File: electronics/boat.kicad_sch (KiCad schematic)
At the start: 22 parts, among them J2 UART1, M5 SG90 9g Micro Servo, M9 WaterPump_DC_DelavanAgPumpsDi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, SW1 Reset, U11 TLE5206-2S, U2 PIC32MX170F256B

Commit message: gate and water pump schematic updated according to wiring
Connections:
- net ConnectionIndicatorPWM4: now also U2.6 (RB2); no longer U2.9 (RA2)
- net GatePWM3: no longer U2.10 (RA3)
- new net GatePWM5: U2.9 (RA2)
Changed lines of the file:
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@@
+	)
+	(no_connect
+		(at 50.8 73.66)
 	)
 	(no_connect
@@
 	)
 	(no_connect
-		(at 90.17 62.23)
-	)
-	(no_connect
 		(at 198.12 90.17)
 	)
@@
 	(wire
 		(pts
+			(xy 114.046 69.85) (xy 118.11 69.85)
+		)
+		(stroke
+			(width 0)
+			(type default)
+		)
+	)
+	(wire
+		(pts
+			(xy 127 45.72) (xy 127 52.07)
+		)
+		(stroke
+			(width 0)
+			(type default)
+		)
+	)
+	(wire
+		(pts
+			(xy 48.26 68.58) (xy 50.8 68.58)
+		)
+		(stroke
+			(width 0)
+			(type default)
+		)
+	)
+	(wire
+		(pts
+			(xy 118.11 69.85) (xy 118.11 70.104)
+		)
+		(stroke
+			(width 0)
+			(type default)
+		)
+	)
+	(wire
+		(pts
+			(xy 130.81 25.146) (xy 130.81 49.53)
+		)
+		(stroke
+			(width 0)
+			(type default)
+		)
+	)
+	(wire
+		(pts
+			(xy 231.14 95.25) (xy 231.14 96.52)
+		)
+		(stroke
+			(width 0)
+			(type default)
+		)
+	)
+	(wire
+		(pts
+			(xy 226.06 38.1) (xy 226.06 41.91)
+		)
+		(stroke
+			(width 0)
+			(type default)
+		)
+	)
+	(wire
+		(pts
+			(xy 201.676 138.43) (xy 204.978 138.43)
+		)
+		(stroke
+			(width 0)
+			(type default)
+		)
+	)
+	(wire
+		(pts
+			(xy 50.8 135.89) (xy 50.8 138.43)
+		)
+		(stroke
+			(width 0)
+			(type default)
+		)
+	)
+	(wire
+		(pts
+			(xy 90.17 25.146) (xy 90.17 40.894)
+		)
+		(stroke
+			(width 0)
+			(type default)
+		)
+	)
+	(wire
+		(pts
+			(xy 204.978 143.51) (xy 209.042 143.51)
+		)
+		(stroke
+			(width 0)
+			(type default)
+		)
+	)
+	(wire
+		(pts
+			(xy 228.6 95.25) (xy 228.6 96.52)
+		)
+		(stroke
+			(width 0)
+			(type default)
+		)
+	)
+	(wire
+		(pts
+			(xy 168.91 138.43) (xy 168.91 141.224)
+		)
+		(stroke
+			(width 0)
+			(type default)
+		)
+	)
+	(wire
+		(pts
+			(xy 104.14 156.21) (xy 74.93 156.21)
+		)
+		(stroke
+			(width 0)
+			(type default)
+		)
+	)
+	(wire
+		(pts
 			(xy 48.26 71.12) (xy 50.8 71.12)
 		)
@@
 	(wire
 		(pts
-			(xy 114.046 69.85) (xy 118.11 69.85)
-		)
-		(stroke
-			(width 0)
-			(type default)
-		)
-	)
-	(wire
-		(pts
-			(xy 127 45.72) (xy 127 52.07)
-		)
-		(stroke
-			(width 0)
-			(type default)
-		)
-	)
-	(wire
-		(pts
-			(xy 48.26 68.58) (xy 50.8 68.58)
-		)
-		(stroke
-			(width 0)
-			(type default)
-		)
-	)
-	(wire
-		(pts
-			(xy 118.11 69.85) (xy 118.11 70.104)
-		)
-		(stroke
-			(width 0)
-			(type default)
-		)
-	)
-	(wire
-		(pts
-			(xy 130.81 25.146) (xy 130.81 49.53)
-		)
-		(stroke
-			(width 0)
-			(type default)
-		)
-	)
-	(wire
-		(pts
-			(xy 231.14 95.25) (xy 231.14 96.52)
-		)
-		(stroke
-			(width 0)
-			(type default)
-		)
-	)
-	(wire
-		(pts
-			(xy 226.06 38.1) (xy 226.06 41.91)
-		)
-		(stroke
-			(width 0)
-			(type default)
-		)
-	)
-	(wire
-		(pts
-			(xy 201.676 138.43) (xy 204.978 138.43)
-		)
-		(stroke
-			(width 0)
-			(type default)
-		)
-	)
-	(wire
-		(pts
-			(xy 50.8 135.89) (xy 50.8 138.43)
-		)
-		(stroke
-			(width 0)
-			(type default)
-		)
-	)
-	(wire
-		(pts
-			(xy 90.17 25.146) (xy 90.17 40.894)
-		)
-		(stroke
-			(width 0)
-			(type default)
-		)
-	)
-	(wire
-		(pts
-			(xy 204.978 143.51) (xy 209.042 143.51)
-		)
-		(stroke
-			(width 0)
-			(type default)
-		)
-	)
-	(wire
-		(pts
-			(xy 228.6 95.25) (xy 228.6 96.52)
-		)
-		(stroke
-			(width 0)
-			(type default)
-		)
-	)
-	(wire
-		(pts
-			(xy 168.91 138.43) (xy 168.91 141.224)
-		)
-		(stroke
-			(width 0)
-			(type default)
-		)
-	)
-	(wire
-		(pts
-			(xy 104.14 156.21) (xy 74.93 156.21)
-		)
-		(stroke
-			(width 0)
-			(type default)
-		)
-	)
-	(wire
-		(pts
 			(xy 48.26 156.21) (xy 50.8 156.21)
 		)
@@
 	(wire
 		(pts
-			(xy 48.26 73.66) (xy 50.8 73.66)
-		)
-		(stroke
-			(width 0)
-			(type default)
-		)
-	)
-	(wire
-		(pts
 			(xy 202.946 116.078) (xy 202.946 125.984)
 		)
@@
 		(pts
 			(xy 48.26 133.35) (xy 50.8 133.35)
+		)
+		(stroke
+			(width 0)
+			(type default)
+		)
+	)
+	(wire
+		(pts
+			(xy 90.17 62.23) (xy 92.71 62.23)
 		)
 		(stroke
@@
 		)
 	)
+	(global_label "ConnectionIndicatorPWM4"
+		(shape input)
+		(at 92.71 62.23 0)
+		(fields_autoplaced yes)
+		(effects
+			(font
+				(size 1.27 1.27)
+			)
+			(justify left)
+		)
+		(property "Intersheetrefs" "${INTERSHEET_REFS}"
+			(at 120.0063 62.23 0)
+			(effects
+				(font
+					(size 1.27 1.27)
+				)
+				(justify left)
+				(hide yes)
+			)
+		)
+	)
 	(global_label "RX"
 		(shape output)
@@
 		)
 	)
-	(global_label "ConnectionIndicatorPWM4"
-		(shape input)
-		(at 48.26 71.12 180)
-		(fields_autoplaced yes)
-		(effects
-			(font
-				(size 1.27 1.27)
-			)
-			(justify right)
-		)
-		(property "Intersheetrefs" "${INTERSHEET_REFS}"
-			(at 20.9637 71.12 0)
-			(effects
-				(font
-					(size 1.27 1.27)
-				)
-				(justify right)
-				(hide yes)
-			)
-		)
-	)
 	(global_label "UART2RX"
 		(shape output)
@@
 		)
 	)
+	(global_label "GatePWM5"
+		(shape input)
+		(at 48.26 71.12 180)
+		(fields_autoplaced yes)
+		(effects
+			(font
+				(size 1.27 1.27)
+			)
+			(justify right)
+		)
+		(property "Intersheetrefs" "${INTERSHEET_REFS}"
+			(at 35.6592 71.12 0)
+			(effects
+				(font
+					(size 1.27 1.27)
+				)
+				(justify right)
+				(hide yes)
+			)
+		)
+	)
 	(global_label "ConnectionIndicatorPWM4"
 		(shape output)
@@
 			(effects
 				(font
-					(size 1.27 1.27)
-				)
-				(justify right)
-				(hide yes)
-			)
-		)
-	)
-	(global_label "GatePWM3"
-		(shape input)
-		(at 48.26 73.66 180)
-		(fields_autoplaced yes)
-		(effects
-			(font
-				(size 1.27 1.27)
-			)
-			(justify right)
-		)
-		(property "Intersheetrefs" "${INTERSHEET_REFS}"
-			(at 35.6592 73.66 0)
-			(effects
-				(font

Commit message: water pump schematic updated to be driven by IRLZ34N N-channel MOSFET
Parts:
- removed C24: 470uF, symbol ME218_BaseLib:Cap
- removed C25: 0.1uF, symbol ME218_BaseLib:Cap
- removed U11: TLE5206-2S, TLE5206-2S:TO127P1000X440X1730-7, symbol TLE5206-2S:TLE5206-2S
- added Q1: IRLZ34N, Package_TO_SOT_THT:TO-220-3_Vertical, symbol Transistor_FET:IRLZ34N
- gave numbers to parts that had none: 5
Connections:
- net +14V: now also M9.1 (+)
- net GND: now also Q1.3 (S)
- net WaterPump: now also Q1.1 (G)
- net at M9.2 (-): now also Q1.2 (D)
- no-connect marks 30 -> 29
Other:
- moved on the sheet: M9

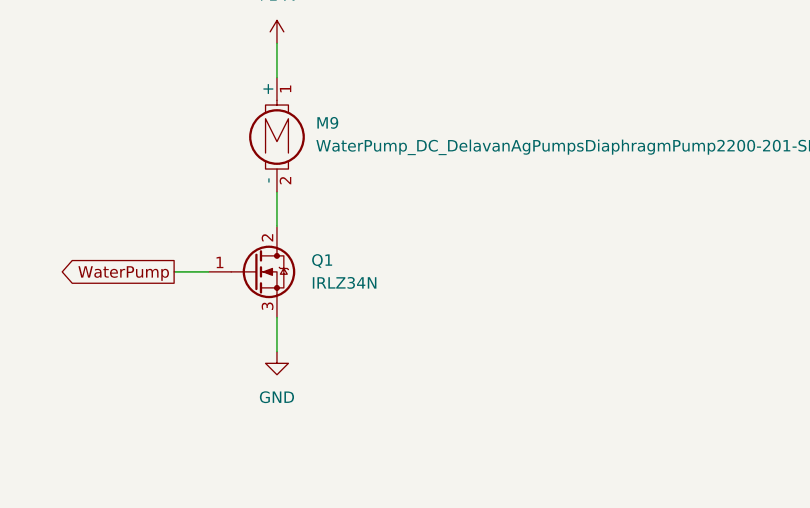
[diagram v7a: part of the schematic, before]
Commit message: updated the schematic to use IRLB3036 over IRLZ34N as it is better for our application (lower conduction loss, better for high current use)
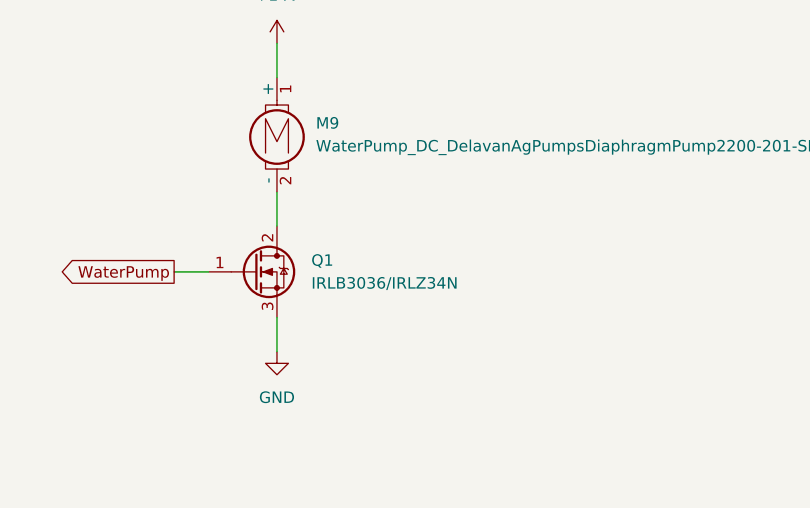
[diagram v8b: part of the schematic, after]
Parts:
- Q1: value IRLZ34N -> IRLB3036/IRLZ34N
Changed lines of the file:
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@@
 	)
 	(image
-		(at 236.22 144.78)
+		(at 246.38 144.78)
 		(scale 0.568723)
 		(data "/9j/4QBsRXhpZgAASUkqAAgAAAADADEBAgAHAAAAMgAAABICAwACAAAAAQABAGmHBAABAAAAOgAA"
@@
 			)
 		)
-		(property "Value" "IRLZ34N"
+		(property "Value" "IRLB3036/IRLZ34N"
 			(at 207.01 144.7799 0)
 			(effects
